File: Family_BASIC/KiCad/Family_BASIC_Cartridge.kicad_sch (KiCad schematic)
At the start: 19 parts, among them IC1 Working RAM (62256), IC2 PRG ROM (27256), IC3 74HCT20, IC4 CHR ROM (27C64), SW1 BACKUP SW, SW2 RAM BANK SW

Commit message: Finalised initial Rev. A design
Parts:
- added JP1: A_{12} Enable, Jumper:SolderJumper-3_P1.3mm_Bridged12_RoundedPad1.0x1.5mm, symbol Jumper:SolderJumper_3_Bridged12
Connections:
- net R/_{W} is gone; now on net R/~{W}: H1.14 (cR~{W})
- net A_{12}: now also JP1.1 (A); no longer IC1.2 (A12)
- net GND: now also JP1.3 (B)
- net SWA_{13} renamed A_{13}SW
- net SWA_{14} renamed A_{14}SW
- new net A_{12}EN: IC1.2 (A12), JP1.2 (C)
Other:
- note removed: "WORK IN PROGRESS"
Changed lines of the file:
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@@
 	(title_block
 		(title "Nintendo Famicom Family BASIC 8KB")
-		(date "27/DEC?2025")
-		(rev "WIP")
+		(date "27/DEC/2025")
+		(rev "A")
 		(company "Brett Hallen")
 	)
-	(text "WORK IN PROGRESS"
-		(exclude_from_sim no)
-		(at 241.046 174.498 0)
-		(effects
-			(font
-				(size 5 5)
-			)
-		)
-	)
 	(text_box "Unused gate as using 256Kbit ROM rather than two 128Kbit."
 		(exclude_from_sim no)
@@
 		)
 	)
-	(text_box "8KB working RAM (0x6000-0x7FFF) so 32KB 62256 gives us four possible banks.\nA_{13} and A_{14} are switchable - they are not connected to address bus.\nIf you're not interested in switching banks, using only 8KB, then omit SW2."
+	(text_box "8KB working RAM (0x6000-0x7FFF) so 32KB 62256 gives us four possible banks.\nA_{13} and A_{14} are switchable - they are not connected to address bus.\n\nIf you're not interested in switching banks, using only 8KB, then omit SW2 - A_{13} & A_{14} are pulled high by default.\n\nIf you only want the original 4KB then cut the A_{12}-to-A_{12}EN solder bridge and connect A_{12}EN to GND."
 		(exclude_from_sim no)
-		(at 218.44 40.64 0)
-		(size 46.99 13.97)
+		(at 234.95 17.78 0)
+		(size 46.99 27.94)
 		(margins 0.9525 0.9525 0.9525 0.9525)
 		(stroke
@@
 		)
 	)
-	(text_box "Family BASIC V3 is hard-coded for a maximum of 4KB:\n\nbasicProgram .eq $6006 ; The start of the BASIC program in memory\nbgGetRam     .eq $6c00 {addr/1024} ; region to save bg data with BGGET\nmemoryTop    .eq $6fff ; What FRETOP is set to by default\n\nPossible to increase to 8KB by patching those constants?\n\nbgGetRam     .eq $7c00 {addr/1024} ; region to save bg data with BGGET\nmemoryTop    .eq $7fff ; What FRETOP is set to by default"
+	(text_box "Family BASIC V3 is hard-coded for a maximum of 4KB.\n\nSome modification is required to hard coded values in the ROM to increase from 0x6FFF limit to full 0x7FFF."
 		(exclude_from_sim no)
-		(at 184.15 139.7 0)
-		(size 91.44 24.13)
+		(at 144.78 144.78 0)
+		(size 110.49 7.62)
 		(margins 0.9525 0.9525 0.9525 0.9525)
 		(stroke
@@
 	(wire
 		(pts
+			(xy 260.35 58.42) (xy 261.62 58.42)
+		)
+		(stroke
+			(width 0)
+			(type default)
+		)
+	)
+	(wire
+		(pts
 			(xy 22.86 58.42) (xy 34.29 58.42)
 		)
@@
 	(wire
 		(pts
+			(xy 246.38 58.42) (xy 250.19 58.42)
+		)
+		(stroke
+			(width 0)
+			(type default)
+		)
+	)
+	(wire
+		(pts
 			(xy 39.37 167.64) (xy 60.96 167.64)
 		)
@@
 	(wire
 		(pts
+			(xy 255.27 62.23) (xy 255.27 64.77)
+		)
+		(stroke
+			(width 0)
+			(type default)
+		)
+	)
+	(wire
+		(pts
 			(xy 209.55 83.82) (xy 209.55 86.36)
 		)
@@
 	(wire
 		(pts
-			(xy 168.91 76.2) (xy 177.8 76.2)
-		)
-		(stroke
-			(width 0)
-			(type default)
-		)
-	)
-	(wire
-		(pts
 			(xy 209.55 101.6) (xy 209.55 93.98)
 		)
@@
 	(wire
 		(pts
+			(xy 168.91 76.2) (xy 177.8 76.2)
+		)
+		(stroke
+			(width 0)
+			(type default)
+		)
+	)
+	(wire
+		(pts
 			(xy 125.73 66.04) (xy 134.62 66.04)
 		)
@@
 		)
 	)
-	(label "SWA_{13}"
+	(label "A_{13}SW"
 		(at 170.18 78.74 0)
 		(effects
@@
 		)
 	)
+	(label "A_{12}EN"
+		(at 170.18 76.2 0)
+		(effects
+			(font
+				(size 1.27 1.27)
+			)
+			(justify left bottom)
+		)
+	)
 	(label "D_{4}"
 		(at 205.74 55.88 0)
@@
 		)
 	)
-	(label "A_{12}"
-		(at 172.72 76.2 0)
-		(effects
-			(font
-				(size 1.27 1.27)
-			)
-			(justify left bottom)
-		)
-	)
 	(label "A_{4}"
 		(at 85.09 55.88 0)
@@
 		)
 	)
-	(label "R{slash}_{W}"
+	(label "R{slash}~{W}"
 		(at 26.67 113.03 0)
 		(effects
@@
 		)
 	)
-	(label "SWA_{14}"
+	(label "A_{14}SW"
 		(at 170.18 81.28 0)
 		(effects
@@
 		)
 	)
+	(label "A_{12}EN"
+		(at 255.27 64.77 0)
+		(effects
+			(font
+				(size 1.27 1.27)
+			)
+			(justify left bottom)
+		)
+	)
 	(label "PD_{1}"
 		(at 68.58 91.44 0)
@@
 		)
 	)
+	(label "A_{12}"
+		(at 246.38 58.42 0)
+		(effects
+			(font
+				(size 1.27 1.27)
+			)
+			(justify left bottom)
+		)
+	)
 	(label "D_{3}"
 		(at 205.74 53.34 0)
@@
 		)
 	)
+	(label "GND"
+		(at 261.62 58.42 0)
+		(effects
+			(font
+				(size 1.27 1.27)
+			)
+			(justify left bottom)
+		)
+	)
 	(symbol
 		(lib_id "Device:C")
@@
 					(unit 1)
 				)
+			)
+		)
+	)
+	(symbol
+		(lib_id "Jumper:SolderJumper_3_Bridged12")
+		(at 255.27 58.42 0)
+		(unit 1)
+		(exclude_from_sim no)
+		(in_bom no)
+		(on_board yes)
+		(dnp no)
+		(fields_autoplaced yes)
+		(property "Reference" "JP1"
+			(at 255.27 52.07 0)
+			(effects
+				(font
+					(size 1.27 1.27)
+				)
+			)
+		)
+		(property "Value" "A_{12} Enable"
+			(at 255.27 54.61 0)
+			(effects
+				(font
+					(size 1.27 1.27)
+				)
+			)
+		)
+		(property "Footprint" "Jumper:SolderJumper-3_P1.3mm_Bridged12_RoundedPad1.0x1.5mm"
+			(at 255.27 58.42 0)
+			(effects
+				(font
+					(size 1.27 1.27)
+				)
+				(hide yes)
+			)
+		)
+		(property "Datasheet" "~"
+			(at 255.27 58.42 0)
+			(effects
+				(font
+					(size 1.27 1.27)
+				)
+				(hide yes)
+			)
+		)
+		(property "Description" "3-pole Solder Jumper, pins 1+2 closed/bridged"
+			(at 255.27 58.42 0)
+			(effects
+				(font
+					(size 1.27 1.27)
+				)
+				(hide yes)
+			)
+		)
+		(pin "3"
+		)
+		(pin "1"
+		)
+		(pin "2"
+		)
+		(instances
+			(project ""
+				(path "/d387318e-3d77-436c-8e35-eead167b1d94"
+					(reference "JP1")
+					(unit 1)
+				)

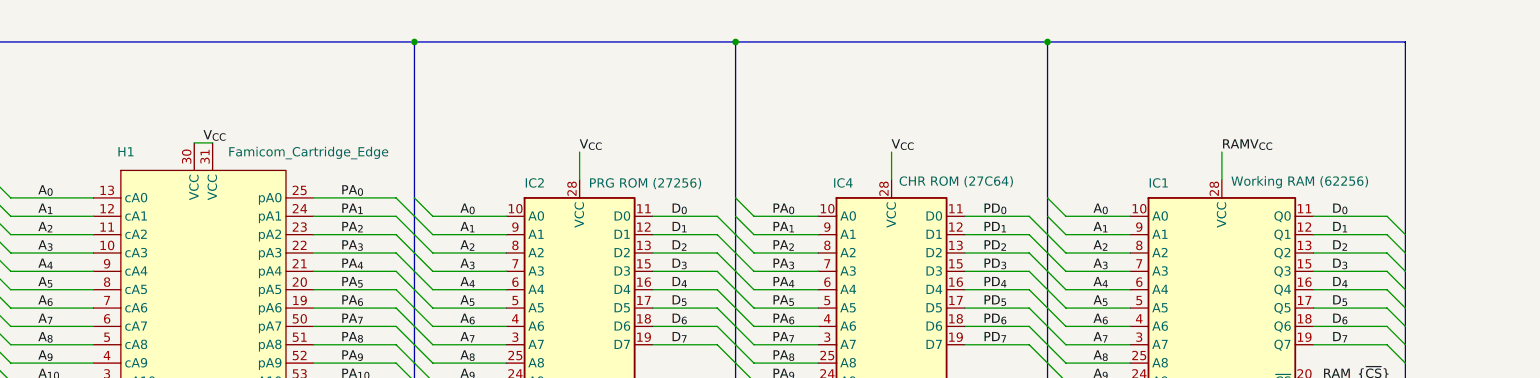
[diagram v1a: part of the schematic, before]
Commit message: Minor cosmetic PCB changes
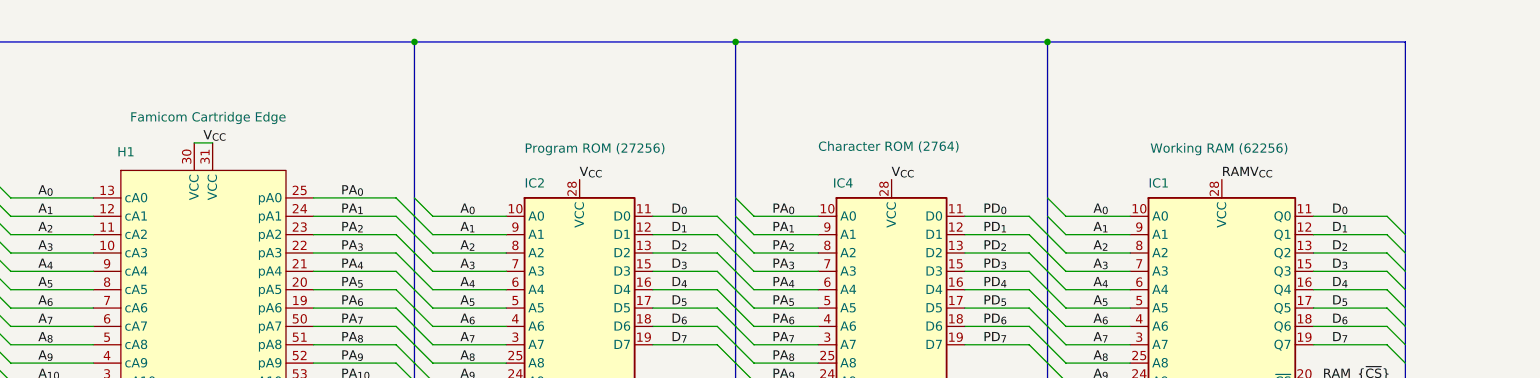
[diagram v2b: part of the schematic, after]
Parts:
- H1: value Famicom_Cartridge_Edge -> Famicom Cartridge Edge
- IC2: value PRG ROM (27256) -> Program ROM (27256)
- IC4: value CHR ROM (27C64) -> Character ROM (2764)
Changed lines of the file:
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@@
 	(wire
 		(pts
-			(xy 190.5 36.83) (xy 190.5 40.64)
-		)
-		(stroke
-			(width 0)
-			(type default)
-		)
-	)
-	(wire
-		(pts
 			(xy 243.84 106.68) (xy 243.84 130.81)
 		)
@@
 	(wire
 		(pts
-			(xy 101.6 36.83) (xy 101.6 40.64)
-		)
-		(stroke
-			(width 0)
-			(type default)
-		)
-	)
-	(wire
-		(pts
 			(xy 81.28 71.12) (xy 91.44 71.12)
 		)
@@
 	(wire
 		(pts
-			(xy 144.78 36.83) (xy 144.78 40.64)
-		)
-		(stroke
-			(width 0)
-			(type default)
-		)
-	)
-	(wire
-		(pts
 			(xy 185.42 101.6) (xy 194.31 101.6)
 		)
@@
 	)
 	(label "RAMV_{CC}"
-		(at 190.5 36.83 0)
+		(at 190.5 40.64 0)
 		(effects
 			(font
@@
 	)
 	(label "V_{CC}"
-		(at 101.6 36.83 0)
+		(at 101.6 40.64 0)
 		(effects
 			(font
@@
 	)
 	(label "V_{CC}"
-		(at 144.78 36.83 0)
+		(at 144.78 40.64 0)
 		(effects
 			(font
@@
 		)
 		(property "Value" "Working RAM (62256)"
-			(at 191.77 40.894 0)
+			(at 180.594 36.322 0)
 			(effects
 				(font
@@
 			)
 		)
-		(property "Value" "CHR ROM (27C64)"
-			(at 145.796 40.894 0)
+		(property "Value" "Character ROM (2764)"
+			(at 134.62 36.068 0)
 			(effects
 				(font
@@
 			)
 		)
-		(property "Value" "PRG ROM (27256)"
-			(at 102.87 41.148 0)
+		(property "Value" "Program ROM (27256)"
+			(at 93.98 36.322 0)
 			(effects
 				(font
@@
 			)
 		)
-		(property "Value" "Famicom_Cartridge_Edge"
-			(at 52.9433 36.83 0)
+		(property "Value" "Famicom Cartridge Edge"
+			(at 39.37 32.004 0)
 			(effects
 				(font

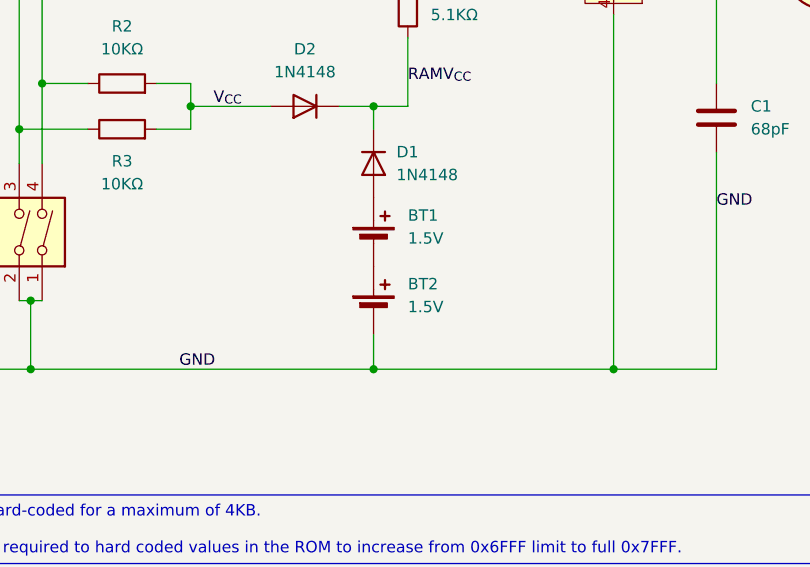
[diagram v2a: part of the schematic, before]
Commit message: Only one button cell holder needed
Each CR2032 button cell is 3V, duh, so only one needed to replace the 2xAA cells.
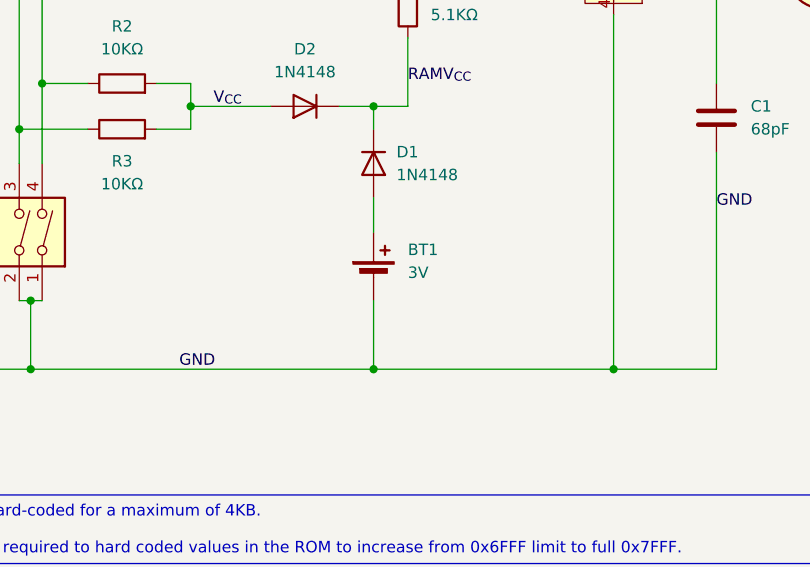
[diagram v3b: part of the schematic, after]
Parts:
- removed BT2: 1.5V, Battery:BatteryHolder_Multicomp_BC-2001_1x2032, symbol Device:Battery_Cell
- BT1: value 1.5V -> 3V; footprint Battery:BatteryHolder_Multicomp_BC-2001_1x2032 -> Clueless_Engineer:3000
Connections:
- net GND: now also BT1.3 (-)
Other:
- moved on the sheet: BT1
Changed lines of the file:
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@@
 	(wire
 		(pts
+			(xy 205.74 115.57) (xy 205.74 111.76)
+		)
+		(stroke
+			(width 0)
+			(type default)
+		)
+	)
+	(wire
+		(pts
 			(xy 81.28 73.66) (xy 91.44 73.66)
 		)
@@
 	(wire
 		(pts
-			(xy 205.74 127) (xy 205.74 130.81)
+			(xy 205.74 123.19) (xy 205.74 130.81)
 		)
 		(stroke
@@
 	(symbol
 		(lib_id "Device:Battery_Cell")
-		(at 205.74 116.84 0)
+		(at 205.74 120.65 0)
 		(unit 1)
 		(exclude_from_sim no)
@@
 		(fields_autoplaced yes)
 		(property "Reference" "BT1"
-			(at 209.55 113.7284 0)
+			(at 209.55 117.5384 0)
 			(effects
 				(font
@@
 			)
 		)
-		(property "Value" "1.5V"
-			(at 209.55 116.2684 0)
+		(property "Value" "3V"
+			(at 209.55 120.0784 0)
 			(effects
 				(font
@@
 			)
 		)
-		(property "Footprint" "Battery:BatteryHolder_Multicomp_BC-2001_1x2032"
-			(at 205.74 115.316 90)
+		(property "Footprint" "Clueless_Engineer:3000"
+			(at 195.58 118.11 90)
 			(effects
 				(font
@@
 		)
 		(property "Datasheet" "~"
-			(at 205.74 115.316 90)
+			(at 205.74 119.126 90)
 			(effects
 				(font
@@
 		)
 		(property "Description" "Single-cell battery"
-			(at 205.74 116.84 0)
+			(at 205.74 130.81 0)
 			(effects
 				(font
@@
 			)
 		)
-		(pin "2"
+		(pin "3"
 		)
 		(pin "1"
@@
 				)
 			)
-		)
-	)
-	(symbol
-		(lib_id "Device:Battery_Cell")
-		(at 205.74 124.46 0)
-		(unit 1)
-		(exclude_from_sim no)
-		(in_bom yes)
-		(on_board yes)
-		(dnp no)
-		(fields_autoplaced yes)
-		(property "Reference" "BT2"
-			(at 209.55 121.3484 0)
-			(effects
-				(font
-					(size 1.27 1.27)
-				)
-				(justify left)
-			)
-		)
-		(property "Value" "1.5V"
-			(at 209.55 123.8884 0)
-			(effects
-				(font
-					(size 1.27 1.27)
-				)
-				(justify left)
-			)
-		)
-		(property "Footprint" "Battery:BatteryHolder_Multicomp_BC-2001_1x2032"
-			(at 205.74 122.936 90)
-			(effects
-				(font
-					(size 1.27 1.27)
-				)
-				(hide yes)
-			)
-		)
-		(property "Datasheet" "~"
-			(at 205.74 122.936 90)
-			(effects
-				(font
-					(size 1.27 1.27)
-				)
-				(hide yes)
-			)
-		)
-		(property "Description" "Single-cell battery"
-			(at 205.74 124.46 0)
-			(effects
-				(font
-					(size 1.27 1.27)
-				)
-				(hide yes)
-			)
-		)
-		(pin "2"
-		)
-		(pin "1"
-		)
-		(instances
-			(project "Family_BASIC_Cartridge"
-				(path "/d387318e-3d77-436c-8e35-eead167b1d94"
-					(reference "BT2")
-					(unit 1)
-				)
-			)
